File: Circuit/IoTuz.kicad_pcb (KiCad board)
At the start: 2 copper layers, 150 x 95 mm, 100 parts, among them J1 Jack.3.5mm-Mono, P1 ALLIGATOR_X39, P2 BATTERY, P3 USB_5PIN_SHELL, P4 LED_1, P5 LED_2, P8 IRReceiver, Q1 S8050, Q2 S8050, Q202 FDN340P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

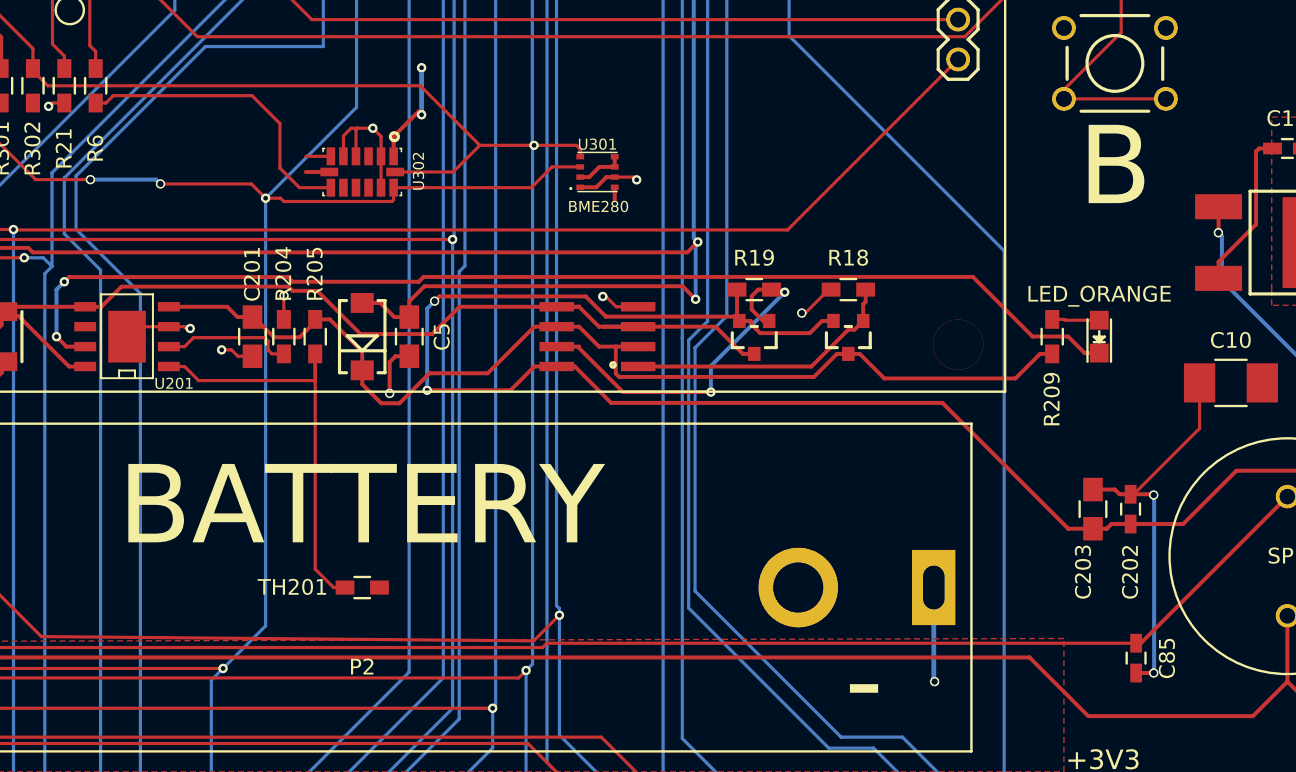
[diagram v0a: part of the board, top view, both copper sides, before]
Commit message: Removed GND from under ADXL
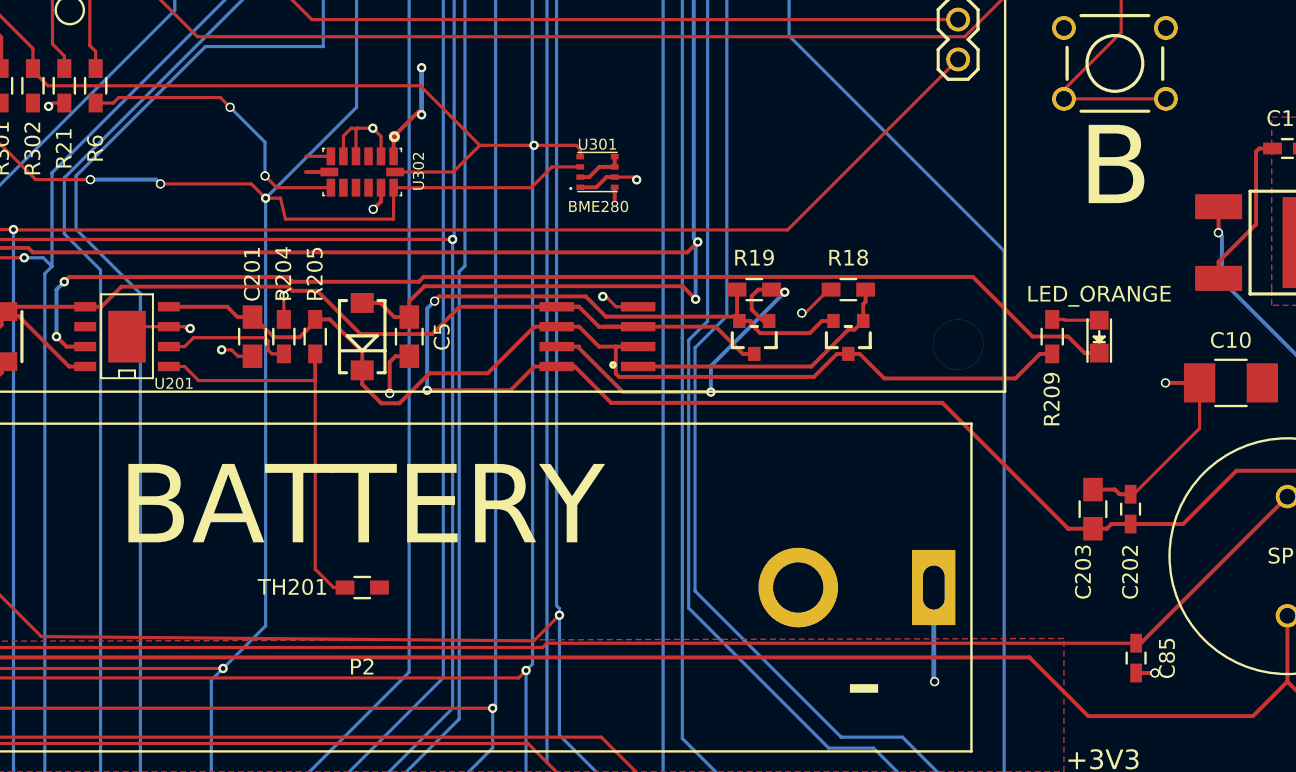
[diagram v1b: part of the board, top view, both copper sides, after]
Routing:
- net GND: track 229.5 -> 218.5 mm, vias 42 -> 43
- net /I2C_SDA: track 197.9 -> 200.1 mm
- net /I2C Sensors/ADXL_INT: track 19.3 -> 18.8 mm, vias 0 -> 2
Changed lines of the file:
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@@
     (thickness 1.6)
     (drawings 219)
-    (tracks 1385)
+    (tracks 1386)
     (zones 0)
     (modules 100)
@@
   (segment (start 124.98 146.242) (end 124.98 142.484) (width 0.2032) (layer F.Cu) (net 0) (status 30))
   (segment (start 122.44 146.242) (end 122.44 142.484) (width 0.2032) (layer F.Cu) (net 0) (status 30))
+  (segment (start 122.9 102.5) (end 121.4 102.5) (width 0.254) (layer F.Cu) (net 1) (status 10))
+  (segment (start 123 101.5) (end 121.4 101.5) (width 0.2032) (layer F.Cu) (net 1) (status 10))
   (segment (start 86 62.9) (end 85.3 62.9) (width 0.254) (layer F.Cu) (net 1))
   (segment (start 76.455 64) (end 74.365 61.91) (width 0.254) (layer F.Cu) (net 1))
@@
   (segment (start 70.9 98.296) (end 71 98.196) (width 0.254) (layer F.Cu) (net 1))
   (segment (start 70.9 99) (end 70.9 98.296) (width 0.254) (layer F.Cu) (net 1) (status 10))
-  (segment (start 123 101.5) (end 121.4 101.5) (width 0.2032) (layer F.Cu) (net 1) (status 10))
   (segment (start 141.1 103.475) (end 141.1 104.3) (width 0.254) (layer F.Cu) (net 1) (status 10))
   (segment (start 87.95 62.9) (end 88.05 63) (width 0.254) (layer F.Cu) (net 1) (status 30))
@@
   (segment (start 127 100.234) (end 128.634 98.6) (width 0.254) (layer F.Cu) (net 1))
   (segment (start 127 101.5) (end 127 100.234) (width 0.254) (layer F.Cu) (net 1) (status 10))
-  (segment (start 122.9 102.5) (end 121.4 102.5) (width 0.254) (layer F.Cu) (net 1) (status 10))
-  (segment (start 174 123.05) (end 175.425 123.05) (width 0.254) (layer F.Cu) (net 2))
-  (segment (start 175.475 134.45) (end 174.35 134.45) (width 0.254) (layer F.Cu) (net 2))
-  (via (at 175.475 134.45) (size 0.6) (drill 0.4) (layers F.Cu B.Cu) (net 2))
-  (segment (start 175.5 134.425) (end 175.475 134.45) (width 0.254) (layer B.Cu) (net 2))
-  (segment (start 175.5 123.125) (end 175.5 134.425) (width 0.254) (layer B.Cu) (net 2))
-  (segment (start 175.475 123.1) (end 175.5 123.125) (width 0.254) (layer B.Cu) (net 2))
-  (via (at 175.475 123.1) (size 0.6) (drill 0.4) (layers F.Cu B.Cu) (net 2))
-  (segment (start 175.425 123.05) (end 175.475 123.1) (width 0.254) (layer F.Cu) (net 2))
+  (segment (start 174.35 134.45) (end 175.55 134.45) (width 0.254) (layer F.Cu) (net 2))
+  (via (at 175.55 134.45) (size 0.6) (drill 0.4) (layers F.Cu B.Cu) (net 2))
+  (segment (start 178.4 115.95) (end 176.225 115.95) (width 0.254) (layer F.Cu) (net 2))
+  (via (at 176.225 115.95) (size 0.6) (drill 0.4) (layers F.Cu B.Cu) (net 2))
+  (via (at 125.7 104.875) (size 0.6) (drill 0.4) (layers F.Cu B.Cu) (net 2))
+  (segment (start 126.2 104.375) (end 125.7 104.875) (width 0.254) (layer F.Cu) (net 2))
+  (segment (start 126.2 103.5) (end 126.2 104.375) (width 0.254) (layer F.Cu) (net 2))
   (segment (start 191.475 59.6) (end 191.475 61.9) (width 0.254) (layer B.Cu) (net 2))
   (segment (start 175.635 60) (end 175.635 61.84) (width 0.254) (layer B.Cu) (net 2))
@@
   (segment (start 174.32 68.05) (end 174.024 67.7545) (width 0.2032) (layer F.Cu) (net 2))
   (segment (start 175 68.05) (end 174.32 68.05) (width 0.2032) (layer F.Cu) (net 2) (status 10))
-  (segment (start 126.2 101.5) (end 126.2 103.5) (width 0.2032) (layer F.Cu) (net 2) (status 30))
   (via (at 68.2546 104.183) (size 0.6) (layers F.Cu B.Cu) (net 3))
   (via (at 146.26 110.615) (size 0.6) (layers F.Cu B.Cu) (net 3))
@@
   (segment (start 106.135 113.635) (end 105.5 113) (width 0.254) (layer F.Cu) (net 72))
   (segment (start 107.333 113.635) (end 106.135 113.635) (width 0.254) (layer F.Cu) (net 72) (status 10))
-  (segment (start 108 98.1) (end 108.6532 98.1) (width 0.2032) (layer F.Cu) (net 73) (status 10))
-  (segment (start 108.6532 98.1) (end 109.120916 97.632284) (width 0.2032) (layer F.Cu) (net 73))
-  (segment (start 119.75 102.25) (end 121 103.5) (width 0.2032) (layer F.Cu) (net 73))
-  (segment (start 109.120916 97.632284) (end 117.970307 97.632284) (width 0.2032) (layer F.Cu) (net 73))
-  (segment (start 121 103.5) (end 123 103.5) (width 0.2032) (layer F.Cu) (net 73) (status 20))
-  (segment (start 117.970307 97.632284) (end 119.75 99.411977) (width 0.2032) (layer F.Cu) (net 73))
-  (segment (start 119.75 99.411977) (end 119.75 102.25) (width 0.2032) (layer F.Cu) (net 73))
+  (segment (start 108 98.1) (end 109.125 98.1) (width 0.2032) (layer F.Cu) (net 73))
+  (segment (start 119.55 103.5) (end 123 103.5) (width 0.2032) (layer F.Cu) (net 73))
+  (segment (start 118.8 102.75) (end 119.55 103.5) (width 0.2032) (layer F.Cu) (net 73))
+  (via (at 118.8 102.75) (size 0.6) (drill 0.4) (layers F.Cu B.Cu) (net 73))
+  (segment (start 118.8 100.6) (end 118.8 102.75) (width 0.2032) (layer B.Cu) (net 73))
+  (segment (start 116.575 98.375) (end 118.8 100.6) (width 0.2032) (layer B.Cu) (net 73))
+  (via (at 116.575 98.375) (size 0.6) (drill 0.4) (layers F.Cu B.Cu) (net 73))
+  (segment (start 115.95 97.75) (end 116.575 98.375) (width 0.2032) (layer F.Cu) (net 73))
+  (segment (start 109.475 97.75) (end 115.95 97.75) (width 0.2032) (layer F.Cu) (net 73))
+  (segment (start 109.125 98.1) (end 109.475 97.75) (width 0.2032) (layer F.Cu) (net 73))
   (segment (start 112.131703 103.261446) (end 117.929446 103.261446) (width 0.2032) (layer F.Cu) (net 74))
   (segment (start 117.929446 103.261446) (end 118.838 104.17) (width 0.2032) (layer F.Cu) (net 74))
@@
   (via (at 124.636 77.5766) (size 0.6) (layers F.Cu B.Cu) (net 74))
   (segment (start 119.79 104.17) (end 118.838 104.17) (width 0.2032) (layer F.Cu) (net 74))
-  (segment (start 120 104.38) (end 119.79 104.17) (width 0.2032) (layer F.Cu) (net 74))
-  (segment (start 126.896 104.38) (end 120 104.38) (width 0.2032) (layer F.Cu) (net 74))
-  (segment (start 127 104.276) (end 126.896 104.38) (width 0.2032) (layer F.Cu) (net 74))
+  (segment (start 120.1 105.505) (end 119.79 104.17) (width 0.2032) (layer F.Cu) (net 74))
+  (segment (start 126.996 105.505) (end 120.1 105.505) (width 0.2032) (layer F.Cu) (net 74))
+  (segment (start 127 104.276) (end 126.996 105.505) (width 0.2032) (layer F.Cu) (net 74))
   (segment (start 124.636 98.3721) (end 118.838 104.17) (width 0.2032) (layer B.Cu) (net 74))
   (segment (start 124.636 77.5766) (end 124.636 98.3721) (width 0.2032) (layer B.Cu) (net 74))

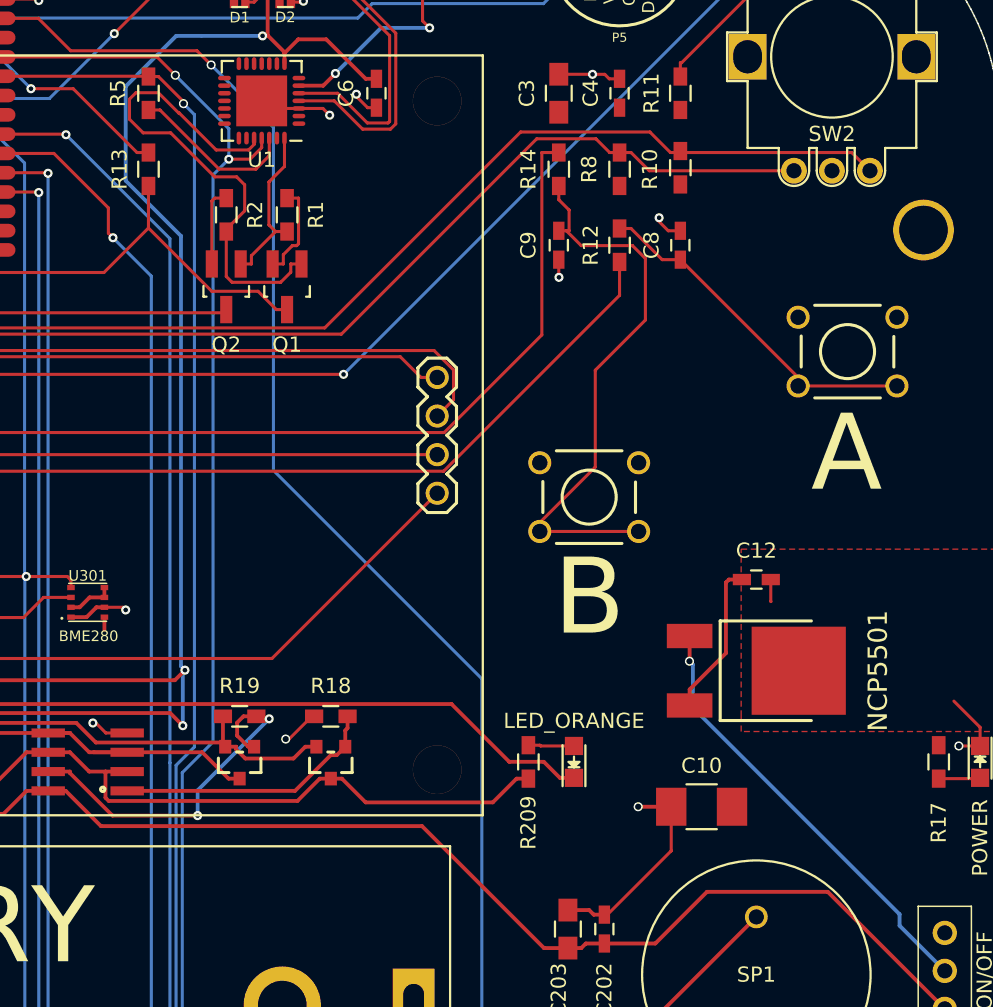
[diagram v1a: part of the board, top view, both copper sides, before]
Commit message: Rerouted tracks for S8050 NPN
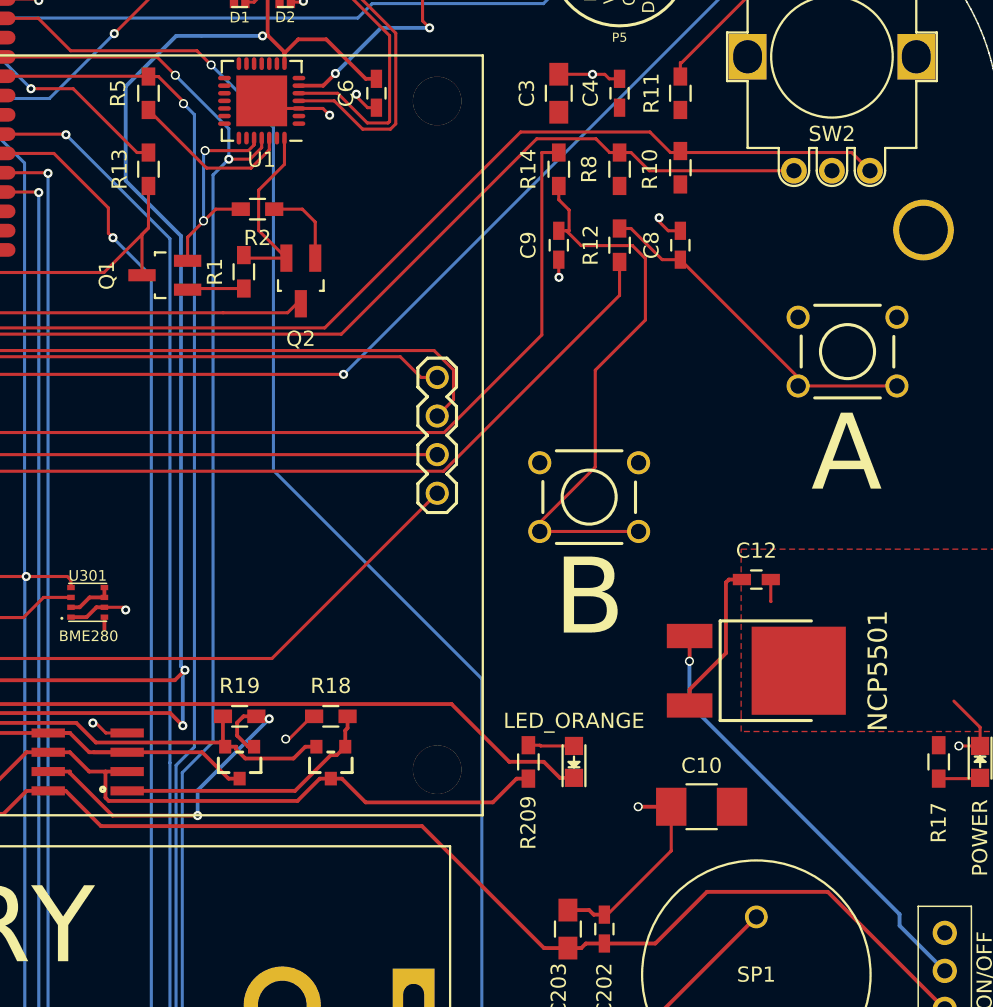
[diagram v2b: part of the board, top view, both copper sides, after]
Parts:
- moved Q1 8.08 mm to (145.1, 81.0), turned to 90 degrees
- moved Q2 4.92 mm to (154.0, 81.3)
- moved R1 4.71 mm to (150.3, 80.8), turned to 90 degrees
- moved R2 2.09 mm to (151.2, 76.6), turned to 180 degrees
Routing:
- net /RTS: track 38.6 -> 14.4 mm, vias 0 -> 2
- net /EN: track 53.2 -> 45.2 mm
- net /IO0: track 162.3 -> 167.4 mm
- net Net-(Q2-Pad1): track 1.46 -> 5.43 mm
- net /DTR: track 14.7 -> 12.2 mm
- net Net-(Q1-Pad1): track 1.46 -> 3.73 mm

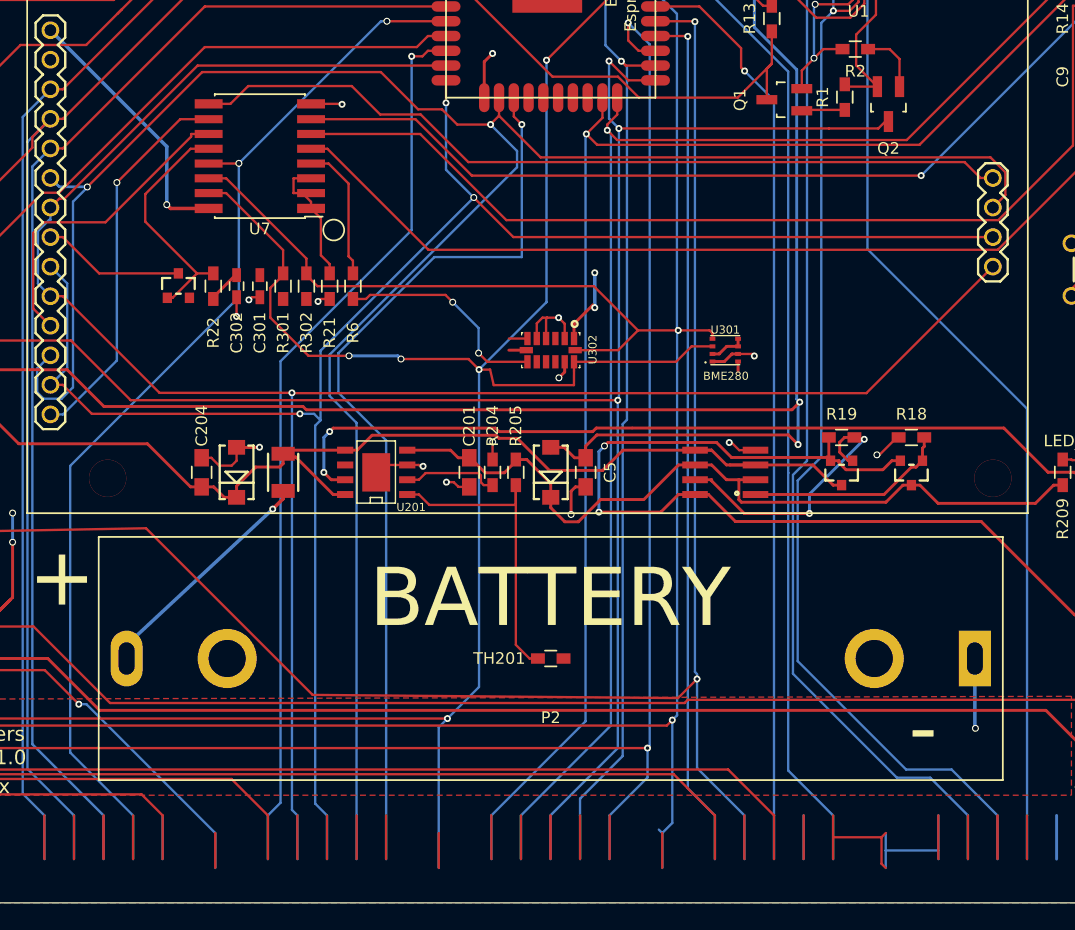
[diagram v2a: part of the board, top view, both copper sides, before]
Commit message: Cleaning up some tracks around 3.3v line.
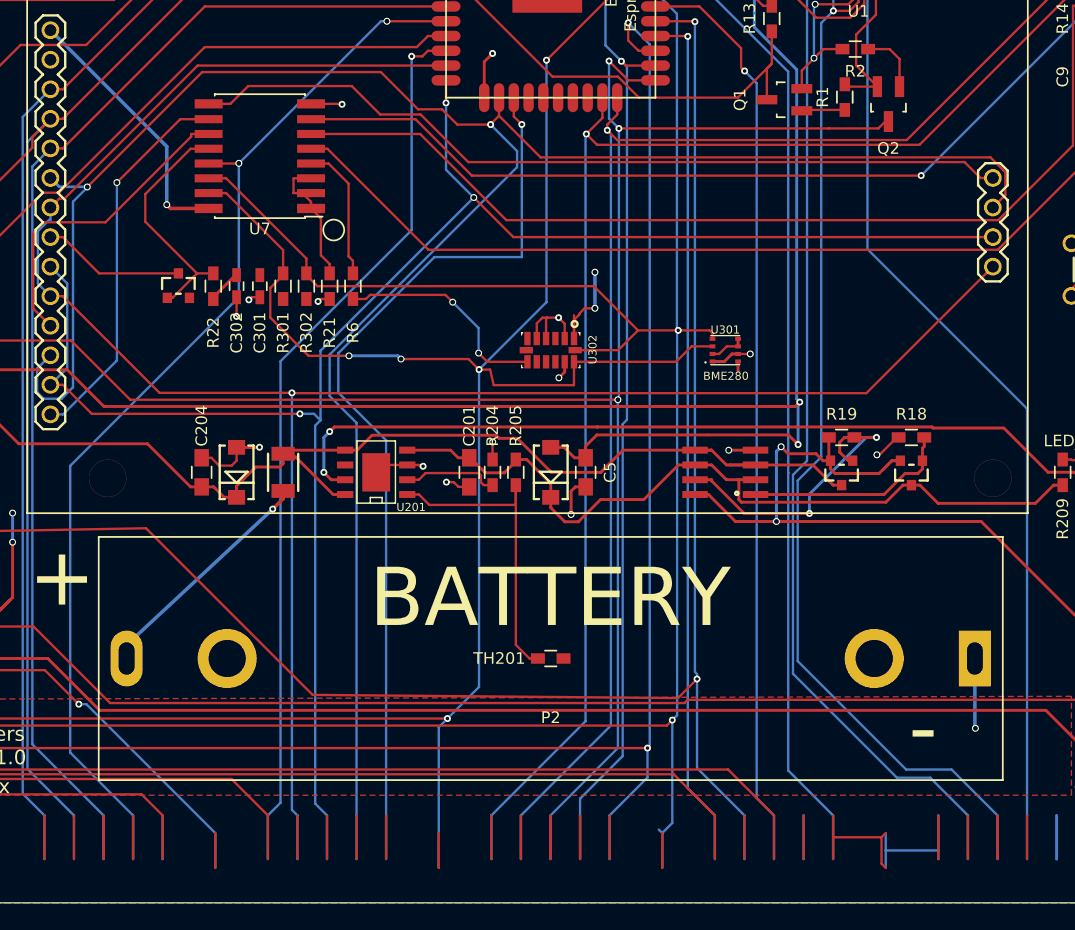
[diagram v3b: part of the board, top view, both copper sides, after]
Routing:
- net /Power/3.3V: track 112.0 -> 91.0 mm
- net /Power/GBAT: track 24.0 -> 26.4 mm
- net /Power/GIN: track 18.0 -> 18.8 mm
- net +3V3: track 143.1 -> 142.4 mm
- net GND: track 218.5 -> 217.9 mm
